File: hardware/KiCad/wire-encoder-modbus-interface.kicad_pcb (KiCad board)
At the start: 2 copper layers, 80 x 80 mm, 27 parts, among them J1 MODBUS-P1, J2 Programming, J3 MODBUS-P2, U1 CH32V003J4M6, U2 MAX3485

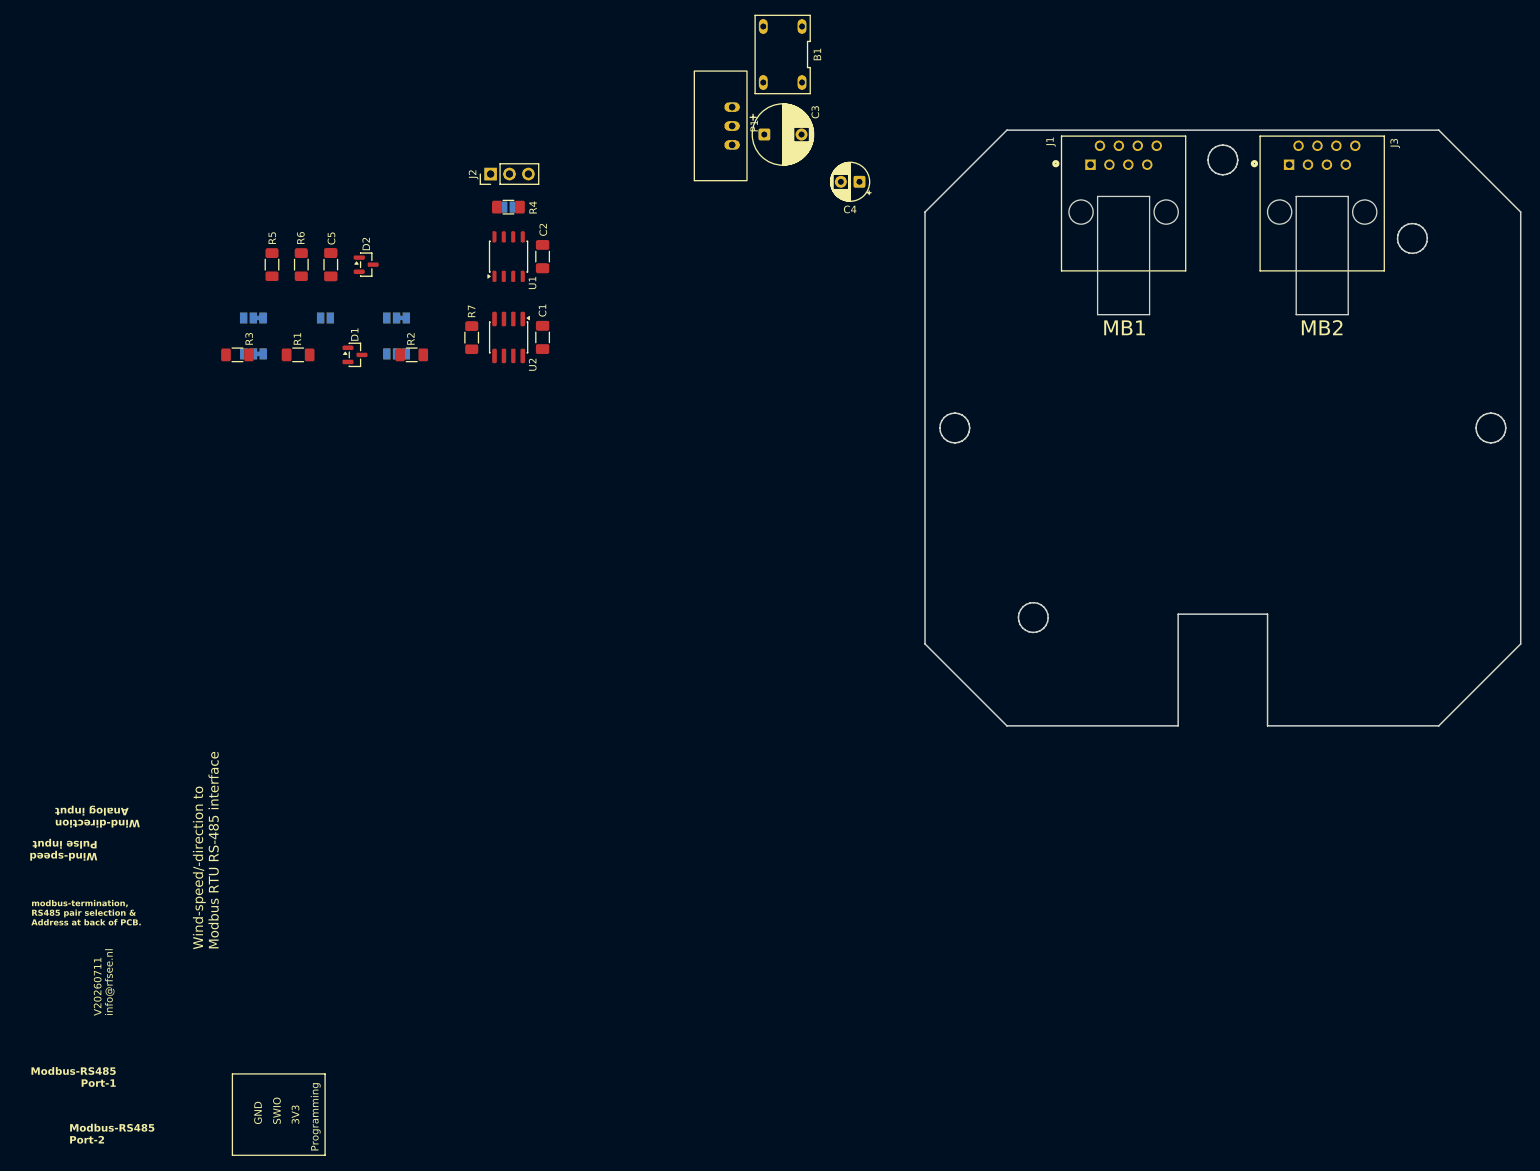
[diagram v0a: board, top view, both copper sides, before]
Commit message: Point the library submodule at master, which has the missing parts
The submodule was pinned to fdb4bd7 on main, whose my-KiCad-library.kicad_sym
carries 22 symbols and lacks both DB207 and HLK-K7803-500R3. Its .pretty
directory lacks the DB207-DIP-4 and HLK-K7803-500R3 footprints as well. The
schematic and board opened regardless, because KiCad caches symbol and
footprint definitions inline in the .kicad_sch and .kicad_pcb -- so the gap
was invisible until Update Symbols from Library, and a fresh clone would have
got a design whose bridge rectifier and buck regulator could not be resolved
from any library.

master at 1ebcfbc has all four, committed and pushed. The move is purely
additive: git diff --numstat fdb4bd7..1ebcfbc shows insertions only, and no
file present at main is absent from master.

All six library items the design references -- DB207, HLK-K7803-500R3 and
215877-1 as symbols, CONN_215877-1, DB207-DIP-4 and HLK-K7803-500R3 as
footprints -- now resolve from the submodule's own history rather than from
untracked files on one disk.
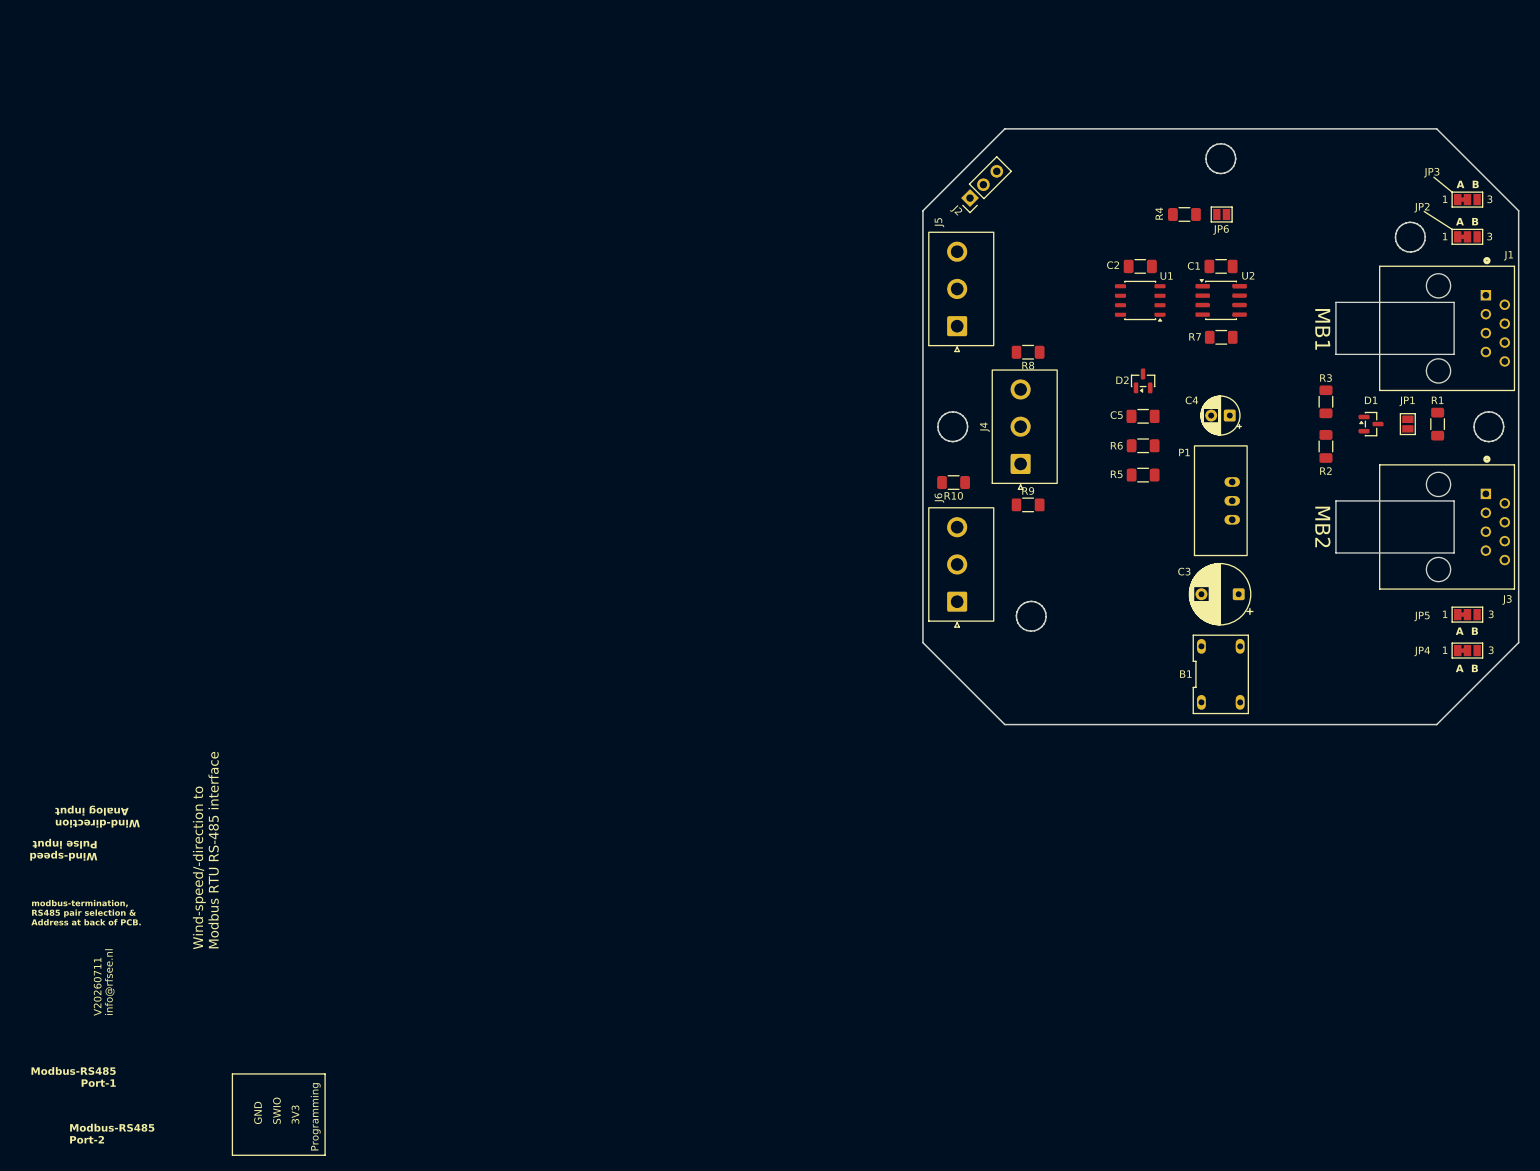
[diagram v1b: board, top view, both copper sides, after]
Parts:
- added J4: Draw-wire, Connector_JST:JST_NV_B03P-NV_1x03_P5.00mm_Vertical, F.Cu at (150.0, 100.5)
- added J5: End switch open, Connector_JST:JST_NV_B03P-NV_1x03_P5.00mm_Vertical, F.Cu at (141.5, 82.0)
- added J6: End switch close, Connector_JST:JST_NV_B03P-NV_1x03_P5.00mm_Vertical, F.Cu at (141.5, 119.0)
- added R10: 470k, Resistor_SMD:R_1206_3216Metric_Pad1.30x1.75mm_HandSolder, F.Cu at (141.0, 103.0)
- added R8: 100k, Resistor_SMD:R_1206_3216Metric_Pad1.30x1.75mm_HandSolder, F.Cu at (151.0, 85.5)
- added R9: 100k, Resistor_SMD:R_1206_3216Metric_Pad1.30x1.75mm_HandSolder, F.Cu at (151.0, 106.0)
- JP1, JP2, JP3, JP4, JP5, JP6: moved to F.Cu
- R5: value 10k -> 4k7
- R6: value 100 -> 10k
- moved JP3 163.8 mm to (210.0, 65.0), turned to 0 degrees
- moved JP2 163.8 mm to (210.0, 70.0), turned to 0 degrees
- moved R1 153.3 mm to (206.0, 95.2), turned to -90 degrees
- moved JP4 149.2 mm to (210.0, 125.6), turned to 0 degrees
- moved JP5 149.2 mm to (210.0, 120.7), turned to 0 degrees
- moved R3 146.3 mm to (191.0, 92.2), turned to 90 degrees
- moved JP1 146.1 mm to (202.0, 95.2), turned to -90 degrees
- moved D1 136.8 mm to (197.1, 95.2)
- moved R2 123.4 mm to (191.0, 98.2), turned to 90 degrees
- moved R5 120.4 mm to (166.4, 102.0), turned to 180 degrees
- moved R6 115.6 mm to (166.4, 98.1), turned to 180 degrees
- moved C5 111.0 mm to (166.4, 94.1), turned to 0 degrees
- moved D2 105.5 mm to (166.4, 89.3), turned to 90 degrees
- moved B1 101.9 mm to (176.9, 128.8), turned to 0 degrees
- moved R7 100.7 mm to (176.9, 83.5), turned to 0 degrees
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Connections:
- C5 pad 2: /PULSE_IN -> /ENDSW
- D2 pad 3: /PULSE_IN -> /ENDSW
- R5 pad 1: /PULSE_IN -> /GND
- R5 pad 2: /3V3 -> /ENDSW
- R6 pad 1: /PULSE_IN -> /ENDSW
- R6 pad 2: unconnected-(R6-Pad2) -> /ENDSW_SUM
- U1 pad 3: /ANALOG_IN -> /WIPER
- U1 pad 5: /PULSE_IN -> /ADDRESS
- U1 pad 7: /ADDRESS -> /ENDSW
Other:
- outline, holes or cut-outs redrawn

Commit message: Final concept PCB-design
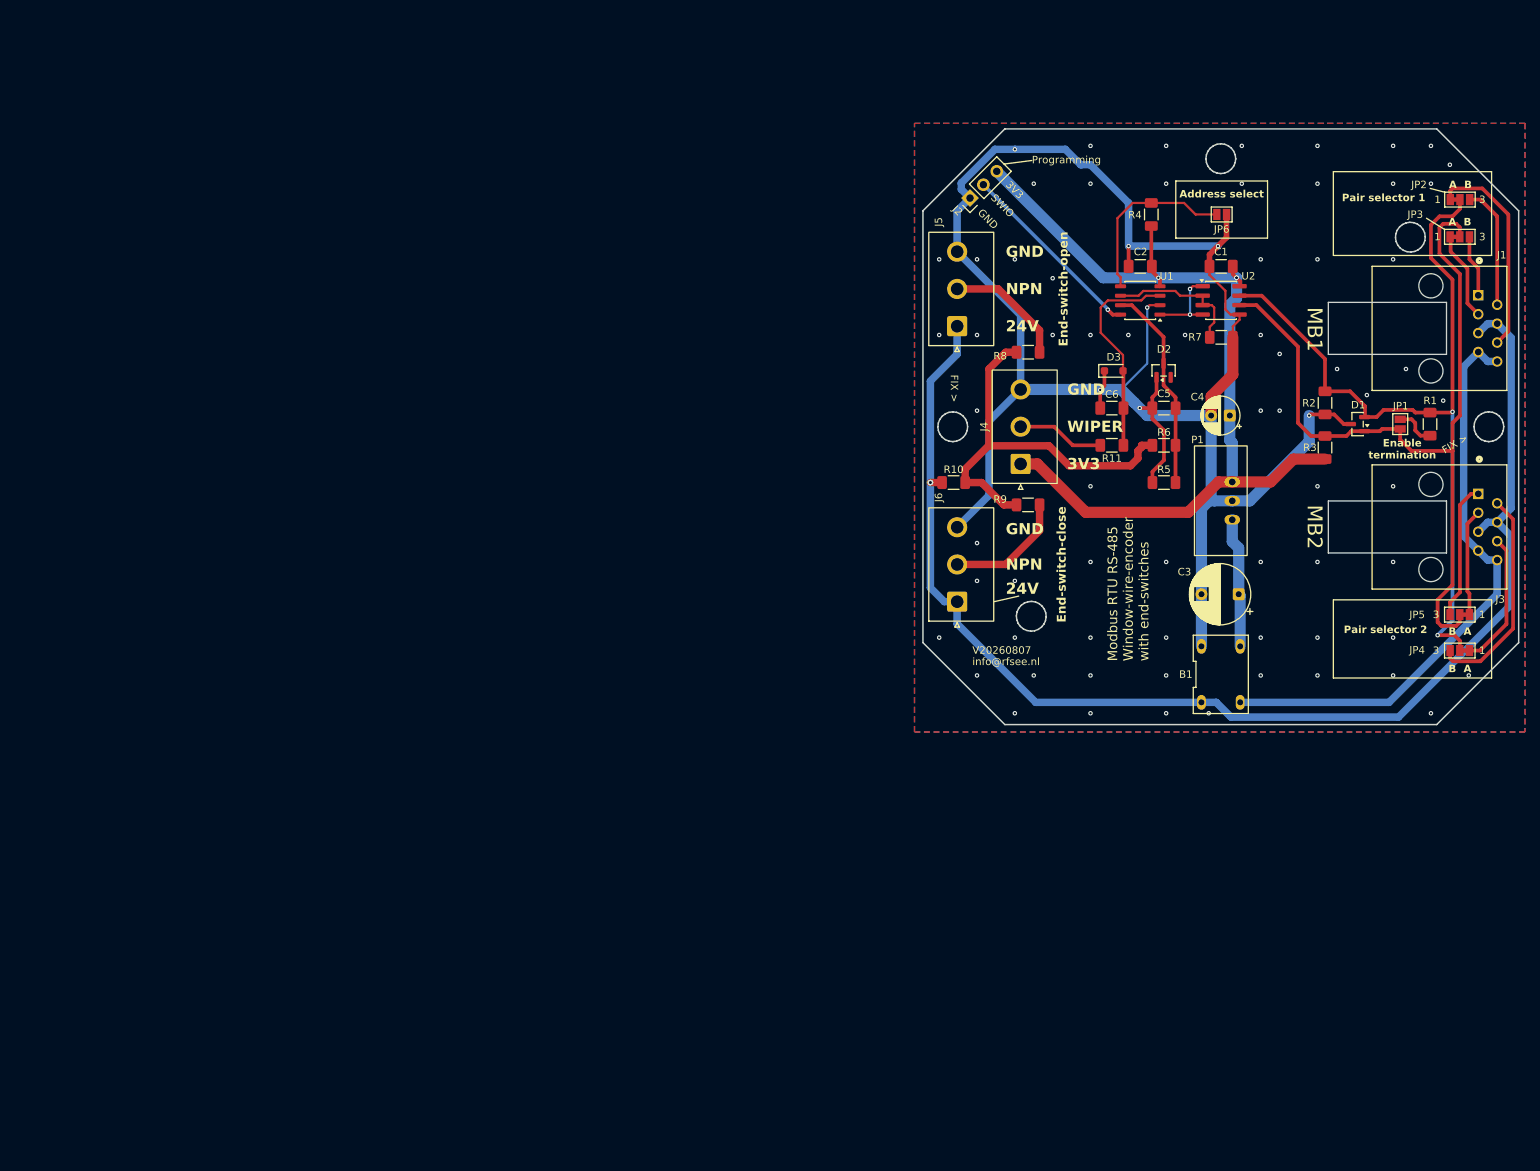
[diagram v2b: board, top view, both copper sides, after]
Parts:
- added C6: 1n, Capacitor_SMD:C_1206_3216Metric_Pad1.33x1.80mm_HandSolder, F.Cu at (162.2, 93.0)
- added D3: TVS >=5V, Diode_SMD:D_SOD-323_HandSoldering, F.Cu at (162.5, 88.0)
- added G***: LOGO_LogoRFSee_37x8mm, my-KiCad-library:LOGO_LogoRFSee_37x8mm, F.Cu at (177.2, 99.5)
- added R11: 10k, Resistor_SMD:R_1206_3216Metric_Pad1.30x1.75mm_HandSolder, F.Cu at (162.2, 98.0)
- moved R3 6.15 mm to (190.9, 98.3)
- moved R2 5.85 mm to (190.9, 92.3), turned to -90 degrees
- moved JP3 5.10 mm to (209.0, 70.0)
- moved JP2 5.10 mm to (209.0, 65.0)
- moved R4 4.45 mm to (167.6, 67.0), turned to -90 degrees
- moved D2 3.09 mm to (169.2, 87.9)
- moved C5 3.01 mm to (169.2, 93.0)
- moved R5 2.97 mm to (169.2, 103.0), turned to 0 degrees
- moved R6 2.80 mm to (169.2, 98.0)
- moved D1 1.81 mm to (195.2, 95.2), turned to 180 degrees
- moved J1 1.02 mm to (205.1, 82.3)
- moved J3 1.02 mm to (205.1, 109.0)
- moved JP1 1.02 mm to (201.0, 95.2)
- moved JP4 1.02 mm to (209.0, 125.6), turned to 180 degrees
- moved JP5 1.02 mm to (209.0, 120.7), turned to 180 degrees
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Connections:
- J4 pad 2: /WIPER -> Net-(J4-Pin_2)
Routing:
- net /GND: track 0.00 -> 255.5 mm, vias 0 -> 74
- net /+24V: track 0.00 -> 177.6 mm, vias 0 -> 1
- net /3V3: track 0.00 -> 124.3 mm, vias 0 -> 3
- net /RS485-A: track 0.00 -> 108.5 mm
- net /RS485-B: track 0.00 -> 107.2 mm, vias 0 -> 2
- net /-24V: track 0.00 -> 79.5 mm
- net /ENDSW_SUM: track 0.00 -> 54.3 mm
- net /_Ab: track 0.00 -> 29.2 mm
- net /WIPER: track 0.00 -> 28.4 mm
- net /Aa: track 0.00 -> 28.4 mm
- net /ENDSW: track 0.00 -> 27.8 mm
- net /SWIO: track 0.00 -> 25.7 mm, vias 0 -> 1
- net /ADDRESS: track 0.00 -> 24.2 mm
- net /MB-RE/DE: track 0.00 -> 18.8 mm
- net /_Bb: track 0.00 -> 18.4 mm
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- added copper zone on B.Cu, net /GND
- added copper zone on F.Cu, net /GND
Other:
- outline, holes or cut-outs redrawn
- board text added: "24V"
- board text added: "End-switch-close"
- board text added: "End-switch-open"
- board text added: "FIX >"
- board text added: "Modbus RTU RS-485 Window-wire-encoder with end-switches"
- board text added: "NPN"
- board text added: "V20260807"
- board text added: "WIPER"
- board text removed: "Modbus-RS485 Port-1"
- board text removed: "Modbus-RS485 Port-2"
- board text removed: "V20260711"
- board text removed: "Wind-direction Analog input"
- board text removed: "Wind-speed Pulse input"
- board text removed: "Wind-speed/-direction to Modbus RTU RS-485 interface"
- board text removed: "modbus-termination, RS485 pair selection & Address at back of PCB."

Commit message: Updated PCB
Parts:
- removed G***: LOGO_LogoRFSee_37x8mm, my-KiCad-library:LOGO_LogoRFSee_37x8mm
- removed R10: 470k, Resistor_SMD:R_1206_3216Metric_Pad1.30x1.75mm_HandSolder
- D3: value TVS >=5V -> PESD5V0S1BA
- R8, R9: value 100k -> 68k
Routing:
- net /ENDSW_SUM: track 54.3 -> 50.4 mm
- net /+24V: track 177.6 -> 176.0 mm, vias 1 -> 0
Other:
- board text added: "V20260901"
- board text removed: "V20260807"

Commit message: Implement the wire-encoder ADC driver, and correct a stale API contract
we.c: the driver everything downstream was blocked on. we.h had been an
API contract with no implementation since July, and integration stage D
cannot start without it.

  we_init          PA2 (ch0, wiper) and PC4 (ch2, end-switch divider) as
                   analog with NO pull; ADC at HCLK/8 = 6 MHz; 73-cycle
                   sample time on both channels; RSTCAL then CAL before any
                   conversion, which is what FR-S18 step 3 exists to order.
  we_sample        FR-E07 integrity check, then 16 conversions with the
                   extreme pair discarded and the middle 14 meaned. FR-E13
                   allows 'mean, or median with outlier rejection'; this is
                   the mean WITH rejection, keeping a mean's sqrt(N) noise
                   reduction while no single glitch can drag the result.
  we_switch_sample same burst on channel 2, no integrity check (see below).
  we_raw_max       1023.

The FR-E07 threshold is derived from the circuit, not chosen. At mid-track
the source is ~12.5 kOhm (2.5 k pot + R11's 10 k) against a ~40 kOhm
internal pull, so a connected wiper shifts ~242 counts between pull-up and
pull-down while an open one swings the full ~1023. The threshold sits at
600, deliberately nearer the open end: a false 'sensor faulty' costs a real
reading.

LIMITATION, and it is a requirement problem not an implementation one:
FR-E07 claims an open OR shorted wiper is detectable by the pull toggle.
A short is not. A field short to GND sits on the far side of R11, so PA2
sees 10 kOhm to 0 V -- electrically identical to the wiper at its bottom
end stop. Same for a short to the top rail. Opens are caught cleanly;
shorts are indistinguishable from a legitimate end-stop reading. Either
FR-E07 is amended or a different scheme is needed.

we.h DOCUMENTED A CIRCUIT THAT HAS NOT EXISTED SINCE 2026-08-29. It
described we_switch_sample as reading a supervised resisto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
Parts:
- added G***: LOGO_LogoRFSee_37x8mm, my-KiCad-library:LOGO_LogoRFSee_37x8mm, F.Cu at (179.2, 69.0)
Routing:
- net /GND: vias 74 -> 78
